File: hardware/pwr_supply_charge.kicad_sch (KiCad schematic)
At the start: 26 parts, among them J1 Battery Input, J2 Power Switch, J3 USB_C_Receptacle_USB2.0_14P, Q1 AO4406A, Q2 AO4406A, Q3 AO4435, Q4 AO4468, U1 HY2120, U2 CN3302

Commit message: Placing components
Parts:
- removed Q4: AO4468, Chromapi_FP:ao4435_SOIC127P600X175-8N, symbol Simulation_SPICE:NMOS
- added Q4: AO4468, Chromapi_FP:ao4435_SOIC127P600X175-8N, symbol Transistor_FET:FDS6630A
- J1: footprint Connector_AMASS:AMASS_XT30PW-M_1x02_P2.50mm_Horizontal -> Connector_AMASS:AMASS_MR30PW-M_1x03_P3.50mm_Horizontal
- L1: footprint Connector_AMASS:AMASS_XT30PW-M_1x02_P2.50mm_Horizontal -> Inductor_SMD:L_7.3x7.3_H3.5
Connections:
- net GND: now also Q4.1 (S), Q4.2 (S), Q4.3 (S)
- net at D1.2 (A), L1.2: now also Q4.5 (D), Q4.6 (D), Q4.7 (D), Q4.8 (D)
- net at U2.5 (LDRV): now also Q4.4 (G)
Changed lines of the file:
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@@
 			)
 		)
-		(property "Footprint" "Connector_AMASS:AMASS_XT30PW-M_1x02_P2.50mm_Horizontal"
+		(property "Footprint" "Connector_AMASS:AMASS_MR30PW-M_1x03_P3.50mm_Horizontal"
 			(at 93.98 38.1 0)
 			(effects
@@
 			)
 		)
-		(property "Footprint" "Connector_AMASS:AMASS_XT30PW-M_1x02_P2.50mm_Horizontal"
+		(property "Footprint" "Inductor_SMD:L_7.3x7.3_H3.5"
 			(at 204.47 97.79 0)
 			(effects
@@
 	)
 	(symbol
-		(lib_id "Simulation_SPICE:NMOS")
+		(lib_id "power:PWR_FLAG")
+		(at 97.79 97.79 0)
+		(unit 1)
+		(exclude_from_sim no)
+		(in_bom yes)
+		(on_board yes)
+		(dnp no)
+		(fields_autoplaced yes)
+		(property "Reference" "#FLG07"
+			(at 97.79 95.885 0)
+			(effects
+				(font
+					(size 1.27 1.27)
+				)
+				(hide yes)
+			)
+		)
+		(property "Value" "PWR_FLAG"
+			(at 97.79 92.71 0)
+			(effects
+				(font
+					(size 1.27 1.27)
+				)
+			)
+		)
+		(property "Footprint" ""
+			(at 97.79 97.79 0)
+			(effects
+				(font
+					(size 1.27 1.27)
+				)
+				(hide yes)
+			)
+		)
+		(property "Datasheet" "~"
+			(at 97.79 97.79 0)
+			(effects
+				(font
+					(size 1.27 1.27)
+				)
+				(hide yes)
+			)
+		)
+		(property "Description" "Special symbol for telling ERC where power comes from"
+			(at 97.79 97.79 0)
+			(effects
+				(font
+					(size 1.27 1.27)
+				)
+				(hide yes)
+			)
+		)
+		(pin "1"
+		)
+		(instances
+			(project "chromapi_motherboard_v1"
+				(path "/d1a31f26-03e0-43e1-89c1-031fe31befc5/2dc5047f-e6b9-4c1e-8ac3-300835122eb4"
+					(reference "#FLG07")
+					(unit 1)
+				)
+			)
+		)
+	)
+	(symbol
+		(lib_id "Transistor_FET:FDS6630A")
 		(at 208.28 113.03 0)
 		(unit 1)
@@
 		)
 		(property "Footprint" "Chromapi_FP:ao4435_SOIC127P600X175-8N"
-			(at 213.36 110.49 0)
-			(effects
-				(font
-					(size 1.27 1.27)
-				)
-				(hide yes)
-			)
-		)
-		(property "Datasheet" "https://github.com/Mowibox/chromapi_motherboard/blob/main/docs/datasheets/AO4458.pdf"
-			(at 208.28 125.73 0)
-			(effects
-				(font
-					(size 1.27 1.27)
-				)
-				(hide yes)
-			)
-		)
-		(property "Description" "30V N-Channel MOSFET"
+			(at 213.36 114.935 0)
+			(effects
+				(font
+					(size 1.27 1.27)
+					(italic yes)
+				)
+				(justify left)
+				(hide yes)
+			)
+		)
+		(property "Datasheet" "https://github.com/Mowibox/chromapi_motherboard/blob/main/docs/datasheets/AO4468.pdf"
+			(at 213.36 116.84 0)
+			(effects
+				(font
+					(size 1.27 1.27)
+				)
+				(justify left)
+				(hide yes)
+			)
+		)
+		(property "Description" "30V, N-Channel MOSFET, SOIC-8"
 			(at 208.28 113.03 0)
 			(effects
@@
 			)
 		)
-		(property "Sim.Device" "NMOS"
-			(at 208.28 130.175 0)
-			(effects
-				(font
-					(size 1.27 1.27)
-				)
-				(hide yes)
-			)
-		)
-		(property "Sim.Type" "VDMOS"
-			(at 208.28 132.08 0)
-			(effects
-				(font
-					(size 1.27 1.27)
-				)
-				(hide yes)
-			)
-		)
-		(property "Sim.Pins" "1=D 2=G 3=S"
-			(at 208.28 128.27 0)
-			(effects
-				(font
-					(size 1.27 1.27)
-				)
-				(hide yes)
-			)
+		(pin "6"
 		)
 		(pin "3"
@@
 		(pin "2"
 		)
-		(pin "1"
+		(pin "8"
+		)
+		(pin "4"
+		)
+		(pin "7"
+		)
+		(pin "1"
+		)
+		(pin "5"
 		)
 		(instances
@@
 					(unit 1)
 				)
-			)
-		)
-	)
-	(symbol
-		(lib_id "power:PWR_FLAG")
-		(at 97.79 97.79 0)
-		(unit 1)
-		(exclude_from_sim no)
-		(in_bom yes)
-		(on_board yes)
-		(dnp no)
-		(fields_autoplaced yes)
-		(property "Reference" "#FLG07"
-			(at 97.79 95.885 0)
-			(effects
-				(font
-					(size 1.27 1.27)
-				)
-				(hide yes)
-			)
-		)
-		(property "Value" "PWR_FLAG"
-			(at 97.79 92.71 0)
-			(effects
-				(font
-					(size 1.27 1.27)
-				)
-			)
-		)
-		(property "Footprint" ""
-			(at 97.79 97.79 0)
-			(effects
-				(font
-					(size 1.27 1.27)
-				)
-				(hide yes)
-			)
-		)
-		(property "Datasheet" "~"
-			(at 97.79 97.79 0)
-			(effects
-				(font
-					(size 1.27 1.27)
-				)
-				(hide yes)
-			)
-		)
-		(property "Description" "Special symbol for telling ERC where power comes from"
-			(at 97.79 97.79 0)
-			(effects
-				(font
-					(size 1.27 1.27)
-				)
-				(hide yes)
-			)
-		)
-		(pin "1"
-		)
-		(instances
-			(project "chromapi_motherboard_v1"
-				(path "/d1a31f26-03e0-43e1-89c1-031fe31befc5/2dc5047f-e6b9-4c1e-8ac3-300835122eb4"
-					(reference "#FLG07")
-					(unit 1)
-				)

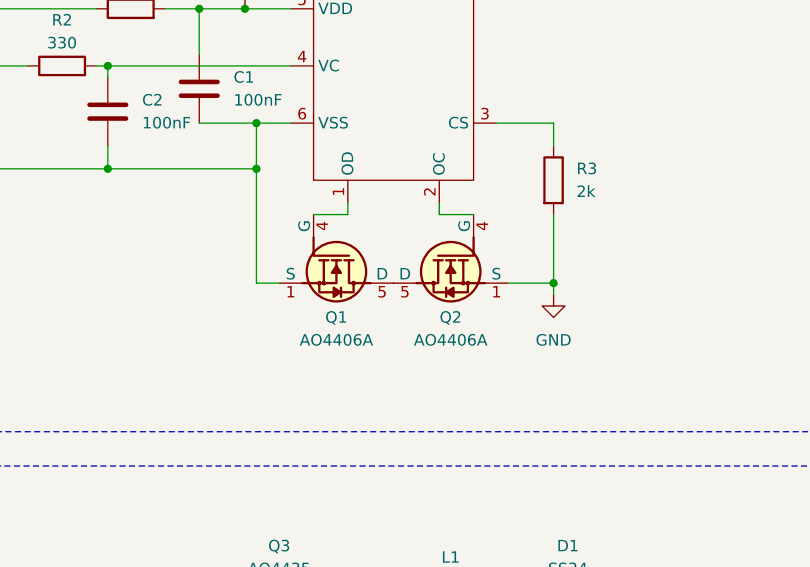
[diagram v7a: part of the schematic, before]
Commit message: Replacing AO4406A by PSMN1R5-30YLC
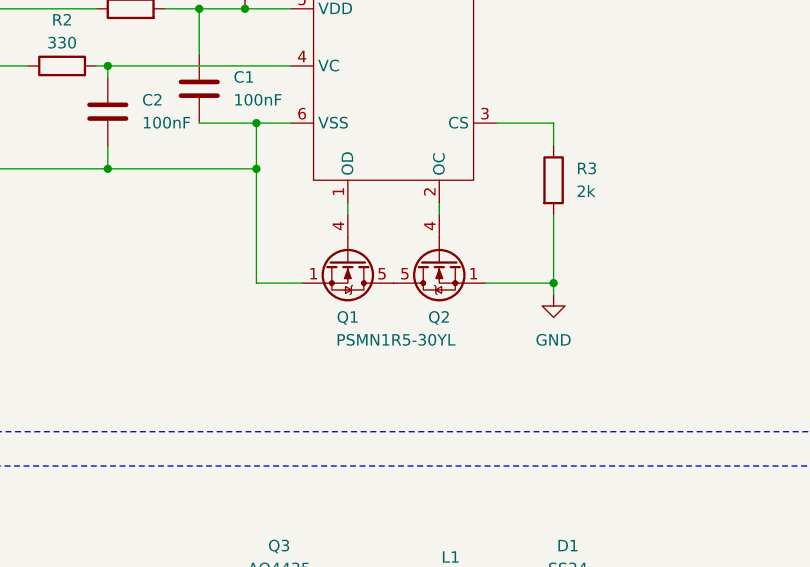
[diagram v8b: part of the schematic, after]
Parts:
- removed Q1, Q2: AO4406A, Chromapi_FP:ao4406a_SOIC-8_3.9x4.9x1.75mm_P1.27mm, symbol ao4406a:AO4406A
- added Q1, Q2: PSMN1R5-30YL, Package_TO_SOT_SMD:LFPAK56, symbol Transistor_FET:PSMN5R2-60YL
- J1: footprint Connector_AMASS:AMASS_MR30PW-M_1x03_P3.50mm_Horizontal -> Connector_JST:JST_XH_B3B-XH-AM_1x03_P2.50mm_Vertical
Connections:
- net B-: now also Q1.1 (S), Q1.2 (S), Q1.3 (S)
- net GND: now also Q2.1 (S), Q2.2 (S), Q2.3 (S)
- net at U1.1 (OD): now also Q1.4 (G)
- net at U1.2 (OC): now also Q2.4 (G)
- new net: Q1.5 (D), Q2.5 (D)
